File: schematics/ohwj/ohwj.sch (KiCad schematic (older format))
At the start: 11 parts

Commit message: Update power and labels; placing labels for all pins
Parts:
- removed C?: 1u, symbol Device:C_Small
- removed C?: 10n, symbol Device:C_Small
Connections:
- net labels added: BTN01, BTN02, BTN03, BTN04, BTN05, BTN06, BTN07, BTN08, BTN09, BTN10, BTN11, BTN12, BTN13, BTN14, BTN15, BTN16, GND, GPIO0, GPIO1, GPIO2, GPIO3, GPIO4, GPIO5, GPIO6, I2C_SCL, I2C_SDA, OSC_IN, OSC_OUT, SPI_MISO, SPI_MOSI, SPI_NSS, SPI_SCK, SWCLK, SWDIO, USART_RX, USART_TX, X0_ADC_IN0, X1_ADC_IN2, Y0_ADC_IN1, Y1_ADC_IN3
- net labels removed: VCC, VCCQ
- wire segments 47 -> 78
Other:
- note removed: "Power input for STM32F030C6 ADC"
- moved on the sheet: C?, D?, R?, SW?

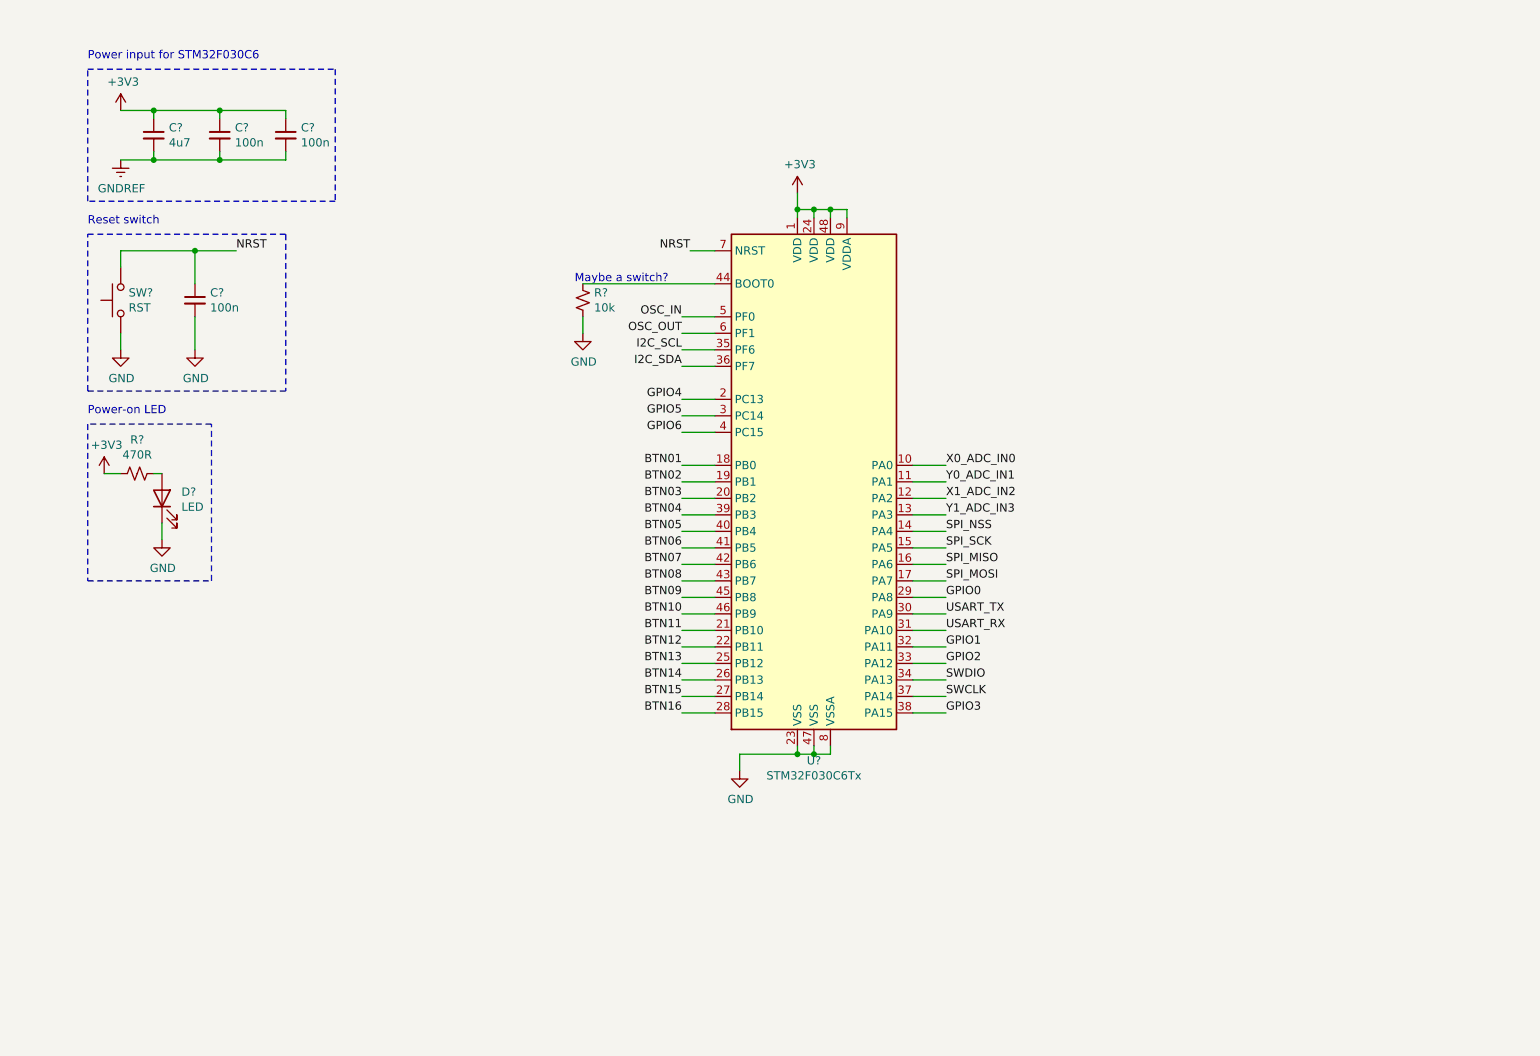
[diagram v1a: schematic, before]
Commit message: Add 8MHz crystal; assing component to pins (reset missing)
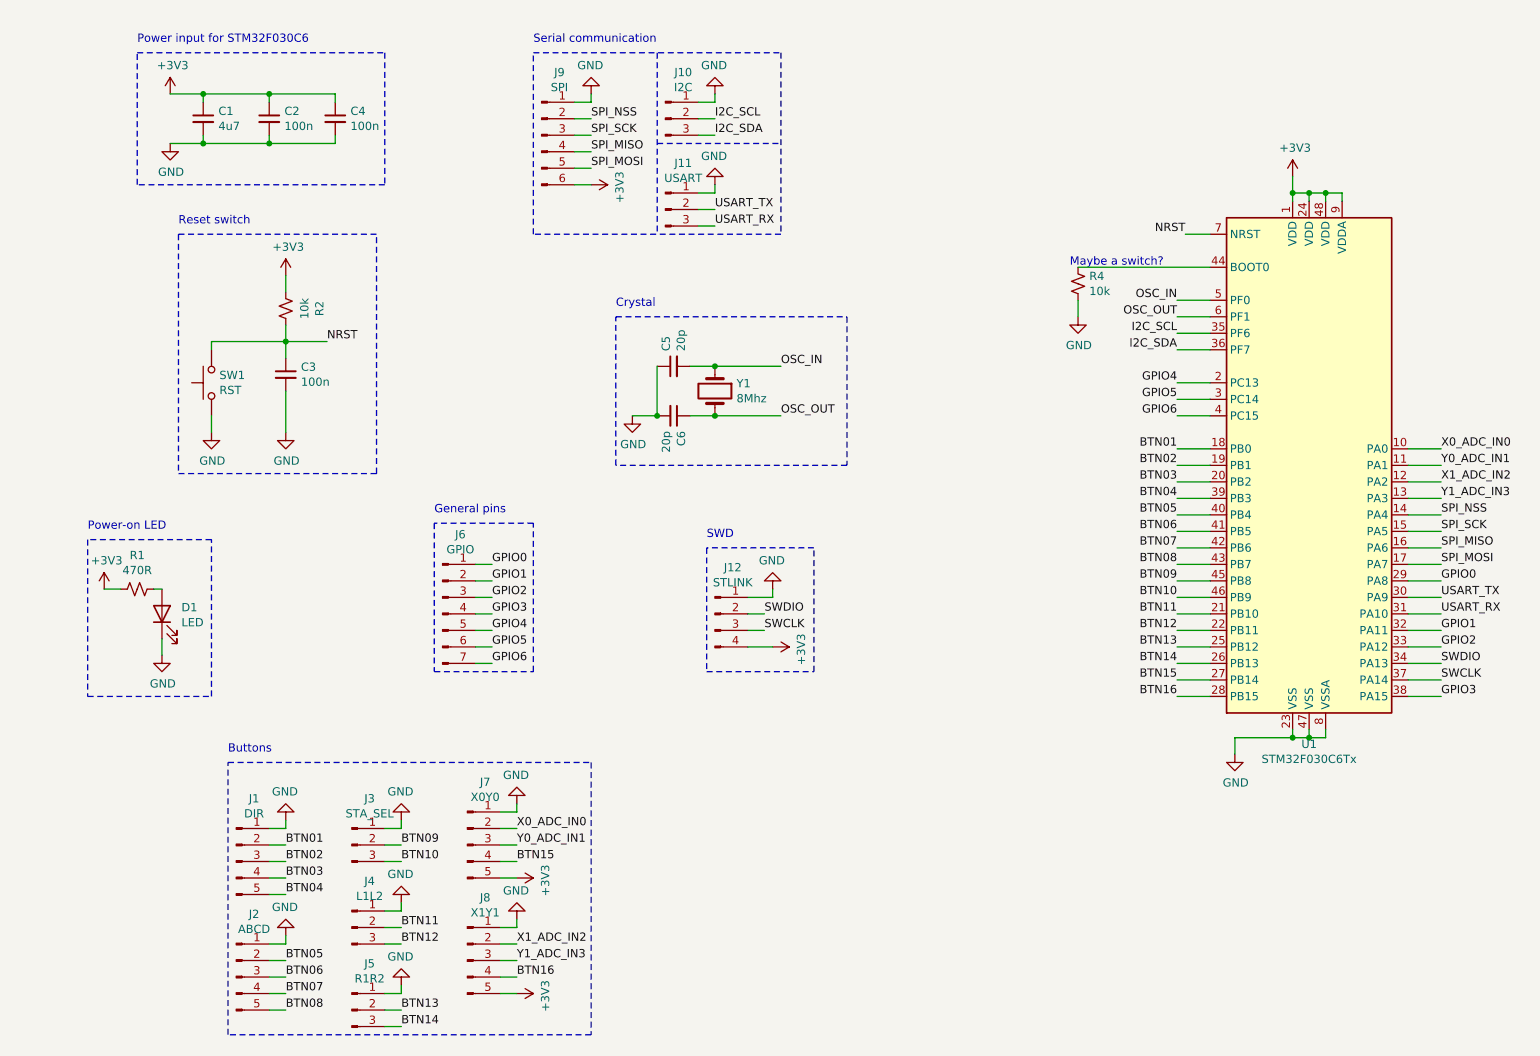
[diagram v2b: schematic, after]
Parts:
- added C5, C6: 20p, Capacitor_SMD:C_0603_1608Metric, symbol Device:C_Small
- added J1: DIR, Connector_PinHeader_2.54mm:PinHeader_1x05_P2.54mm_Vertical, symbol Connector:Conn_01x05_Male
- added J10: I2C, Connector_PinHeader_2.54mm:PinHeader_1x03_P2.54mm_Vertical, symbol Connector:Conn_01x03_Male
- added J11: USART, Connector_PinHeader_2.54mm:PinHeader_1x03_P2.54mm_Vertical, symbol Connector:Conn_01x03_Male
- added J12: STLINK, Connector_PinHeader_2.54mm:PinHeader_1x04_P2.54mm_Vertical, symbol Connector:Conn_01x04_Male
- added J2: ABCD, Connector_PinHeader_2.54mm:PinHeader_1x05_P2.54mm_Vertical, symbol Connector:Conn_01x05_Male
- added J3: STA_SEL, Connector_PinHeader_2.54mm:PinHeader_1x03_P2.54mm_Vertical, symbol Connector:Conn_01x03_Male
- added J4: L1L2, Connector_PinHeader_2.54mm:PinHeader_1x03_P2.54mm_Vertical, symbol Connector:Conn_01x03_Male
- added J5: R1R2, Connector_PinHeader_2.54mm:PinHeader_1x03_P2.54mm_Vertical, symbol Connector:Conn_01x03_Male
- added J6: GPIO, Connector_PinHeader_2.54mm:PinHeader_1x07_P2.54mm_Vertical, symbol Connector:Conn_01x07_Male
- added J7: X0Y0, Connector_PinHeader_2.54mm:PinHeader_1x05_P2.54mm_Vertical, symbol Connector:Conn_01x05_Male
- added J8: X1Y1, Connector_PinHeader_2.54mm:PinHeader_1x05_P2.54mm_Vertical, symbol Connector:Conn_01x05_Male
- added J9: SPI, Connector_PinHeader_2.54mm:PinHeader_1x06_P2.54mm_Vertical, symbol Connector:Conn_01x06_Male
- added R2: 10k, Resistor_SMD:R_0603_1608Metric, symbol Device:R_Small_US
- added Y1: 8Mhz, Crystal:Crystal_HC49-4H_Vertical, symbol Device:Crystal
- C1, C2, C3, C4: renamed from C?; footprint (none) -> Capacitor_SMD:C_0603_1608Metric
- D1: renamed from D?; footprint (none) -> LED_SMD:LED_0603_1608Metric
- R1, R4: renamed from R?; footprint (none) -> Resistor_SMD:R_0603_1608Metric
- gave numbers to parts that had none: 2
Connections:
- net GNDREF is gone; now on net GND: C1.2, C2.2, C4.2
- net +3V3: now also J12.4 (Pin_4), J7.5 (Pin_5), J8.5 (Pin_5), J9.6 (Pin_6), R2.1
- net BTN01: now also J1.2 (Pin_2)
- net BTN02: now also J1.3 (Pin_3)
- net BTN03: now also J1.4 (Pin_4)
- net BTN04: now also J1.5 (Pin_5)
- net BTN05: now also J2.2 (Pin_2)
- net BTN06: now also J2.3 (Pin_3)
- net BTN07: now also J2.4 (Pin_4)
- net BTN08: now also J2.5 (Pin_5)
- net BTN09: now also J3.2 (Pin_2)
- net BTN10: now also J3.3 (Pin_3)
- net BTN11: now also J4.2 (Pin_2)
- net BTN12: now also J4.3 (Pin_3)
- net BTN13: now also J5.2 (Pin_2)
- net BTN14: now also J5.3 (Pin_3)
- net BTN15: now also J7.4 (Pin_4)
- net BTN16: now also J8.4 (Pin_4)
- net GND: now also C5.1, C6.2, J1.1 (Pin_1), J10.1 (Pin_1), J11.1 (Pin_1), J12.1 (Pin_1), J2.1 (Pin_1), J3.1 (Pin_1), J4.1 (Pin_1), J5.1 (Pin_1), J7.1 (Pin_1), J8.1 (Pin_1), J9.1 (Pin_1)
- net GPIO0: now also J6.1 (Pin_1)
- net GPIO1: now also J6.2 (Pin_2)
- net GPIO2: now also J6.3 (Pin_3)
- net GPIO3: now also J6.4 (Pin_4)
- net GPIO4: now also J6.5 (Pin_5)
- net GPIO5: now also J6.6 (Pin_6)
- net GPIO6: now also J6.7 (Pin_7)
- net I2C_SCL: now also J10.2 (Pin_2)
- net I2C_SDA: now also J10.3 (Pin_3)
- net NRST: now also R2.2
- net OSC_IN: now also C5.2, Y1.1
- net OSC_OUT: now also C6.1, Y1.2
- net SPI_MISO: now also J9.4 (Pin_4)
- net SPI_MOSI: now also J9.5 (Pin_5)
- net SPI_NSS: now also J9.2 (Pin_2)
- net SPI_SCK: now also J9.3 (Pin_3)
- net SWCLK: now also J12.3 (Pin_3)
- net SWDIO: now also J12.2 (Pin_2)
- net USART_RX: now also J11.3 (Pin_3)
- net USART_TX: now also J11.2 (Pin_2)
- net X0_ADC_IN0: now also J7.2 (Pin_2)
- net X1_ADC_IN2: now also J8.2 (Pin_2)
- net Y0_ADC_IN1: now also J7.3 (Pin_3)
- net Y1_ADC_IN3: now also J8.3 (Pin_3)
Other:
- note added: "Buttons"
- note added: "Crystal"
- note added: "General pins"
- note added: "SWD"
- note added: "Serial communication"
- moved on the sheet: C1, C2, C3, C4, D1, R1, R4, SW1, U1

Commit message: Add voltage regulator; defined all footprints
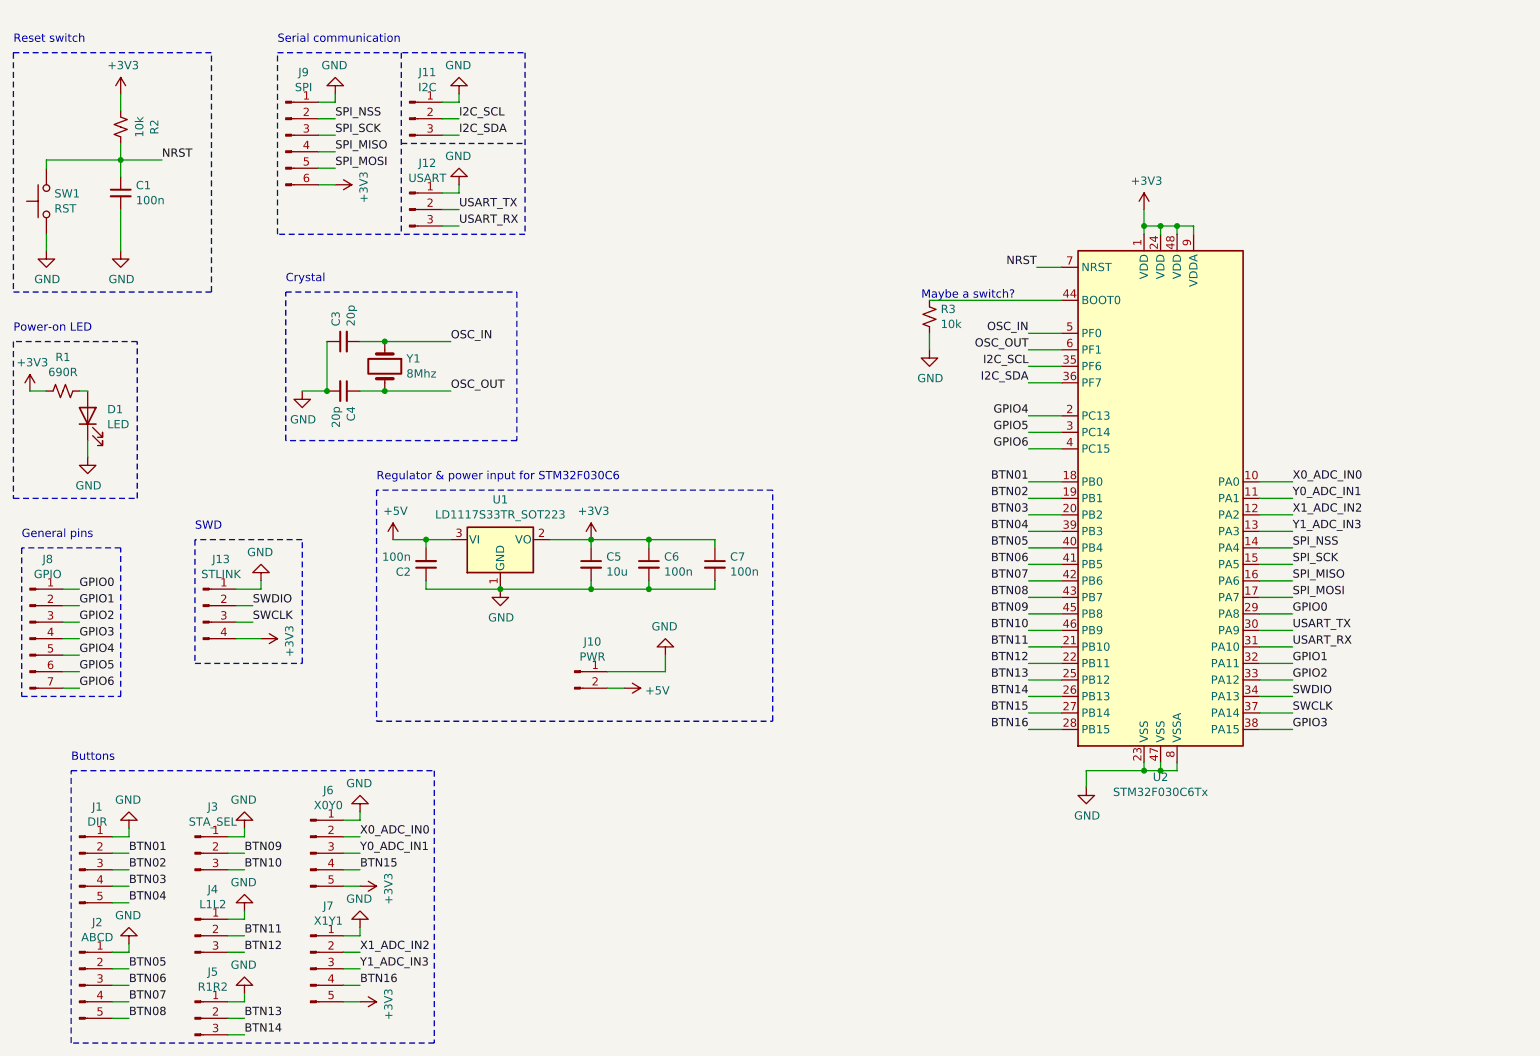
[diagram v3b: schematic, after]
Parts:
- removed C1: 4u7, Capacitor_SMD:C_0603_1608Metric, symbol Device:C_Small
- added C2: 100n, Capacitor_SMD:C_0603_1608Metric, symbol Device:C_Small
- added C5: 10u, Capacitor_SMD:C_0603_1608Metric, symbol Device:C_Small
- added J10: PWR, Connector_PinHeader_2.54mm:PinHeader_1x02_P2.54mm_Vertical, symbol Connector:Conn_01x02_Male
- added U1: LD1117S33TR_SOT223, Package_TO_SOT_SMD:SOT-223-3_TabPin2, symbol Regulator_Linear:LD1117S33TR_SOT223
- R1: value 470R -> 690R
- SW1: footprint (none) -> Button_Switch_THT:SW_PUSH_6mm_H4.3mm
- renumbered C3 to C1, C5 to C3, C6 to C4, C2 to C6, C4 to C7, J10 to J11, J11 to J12, J12 to J13, J7 to J6, J8 to J7, J6 to J8, R4 to R3, U1 to U2
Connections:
- net +3V3: now also C5.1, U1.2 (VO)
- net GND: now also C2.1, C5.2, J10.1 (Pin_1), U1.1 (GND)
- new net +5V: C2.2, J10.2 (Pin_2), U1.3 (VI)
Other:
- note added: "Regulator & power input for STM32F030C6"
- note removed: "Power input for STM32F030C6"
- moved on the sheet: C1, C3, C4, C6, C7, D1, J1, J11, J12, J13, J2, J3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

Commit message: Preliminar PCB layout
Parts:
- removed J1: DIR, Connector_PinHeader_2.54mm:PinHeader_1x05_P2.54mm_Vertical, symbol Connector:Conn_01x05_Male
- removed J11: I2C, Connector_PinHeader_2.54mm:PinHeader_1x03_P2.54mm_Vertical, symbol Connector:Conn_01x03_Male
- removed J12: USART, Connector_PinHeader_2.54mm:PinHeader_1x03_P2.54mm_Vertical, symbol Connector:Conn_01x03_Male
- removed J13: STLINK, Connector_PinHeader_2.54mm:PinHeader_1x04_P2.54mm_Vertical, symbol Connector:Conn_01x04_Male
- removed J2: ABCD, Connector_PinHeader_2.54mm:PinHeader_1x05_P2.54mm_Vertical, symbol Connector:Conn_01x05_Male
- removed J3: STA_SEL, Connector_PinHeader_2.54mm:PinHeader_1x03_P2.54mm_Vertical, symbol Connector:Conn_01x03_Male
- removed J4: L1L2, Connector_PinHeader_2.54mm:PinHeader_1x03_P2.54mm_Vertical, symbol Connector:Conn_01x03_Male
- removed J5: R1R2, Connector_PinHeader_2.54mm:PinHeader_1x03_P2.54mm_Vertical, symbol Connector:Conn_01x03_Male
- removed J6: X0Y0, Connector_PinHeader_2.54mm:PinHeader_1x05_P2.54mm_Vertical, symbol Connector:Conn_01x05_Male
- removed J7: X1Y1, Connector_PinHeader_2.54mm:PinHeader_1x05_P2.54mm_Vertical, symbol Connector:Conn_01x05_Male
- removed J8: GPIO, Connector_PinHeader_2.54mm:PinHeader_1x07_P2.54mm_Vertical, symbol Connector:Conn_01x07_Male
- removed J9: SPI, Connector_PinHeader_2.54mm:PinHeader_1x06_P2.54mm_Vertical, symbol Connector:Conn_01x06_Male
- added J1: SIDE A, Connector_PinHeader_2.54mm:PinHeader_1x06_P2.54mm_Vertical, symbol Connector:Conn_01x06_Male
- added J2: SIDE B, Connector_PinHeader_2.54mm:PinHeader_1x10_P2.54mm_Vertical, symbol Connector:Conn_01x10_Male
- added J3: SIDE C, Connector_PinHeader_2.54mm:PinHeader_1x12_P2.54mm_Vertical, symbol Connector:Conn_01x12_Male
- added J5: SIDE D, Connector_PinHeader_2.54mm:PinHeader_1x09_P2.54mm_Vertical, symbol Connector:Conn_01x09_Male
- renumbered J10 to J4
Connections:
- net BTN01: now also J2.6 (Pin_6)
- net BTN02: now also J2.7 (Pin_7)
- net BTN03: now also J2.8 (Pin_8)
- net BTN04: now also J5.3 (Pin_3)
- net BTN05: now also J5.4 (Pin_4)
- net BTN06: now also J5.5 (Pin_5)
- net BTN07: now also J5.6 (Pin_6)
- net BTN08: now also J5.7 (Pin_7)
- net BTN09: now also J5.8 (Pin_8)
- net BTN10: now also J5.9 (Pin_9)
- net BTN11: now also J2.9 (Pin_9)
- net BTN12: now also J2.10 (Pin_10)
- net BTN13: now also J3.1 (Pin_1)
- net BTN14: now also J3.2 (Pin_2)
- net BTN15: now also J3.3 (Pin_3)
- net BTN16: now also J3.4 (Pin_4)
- net GPIO0: now also J3.5 (Pin_5)
- net GPIO1: now also J3.8 (Pin_8)
- net GPIO2: now also J3.9 (Pin_9)
- net GPIO3: now also J5.2 (Pin_2)
- net SPI_MISO: now also J2.4 (Pin_4)
- net SPI_MOSI: now also J2.5 (Pin_5)
- net SPI_NSS: now also J2.2 (Pin_2)
- net SPI_SCK: now also J2.3 (Pin_3)
- net SWCLK: now also J5.1 (Pin_1)
- net SWDIO: now also J3.10 (Pin_10)
- net X0_ADC_IN0: now also J1.4 (Pin_4)
- net X1_ADC_IN2: now also J1.6 (Pin_6)
- net Y0_ADC_IN1: now also J1.5 (Pin_5)
- net Y1_ADC_IN3: now also J2.1 (Pin_1)
- net GPIO4 renamed PC13
- net PC13: now also J1.1 (Pin_1)
- net GPIO5 renamed PC14
- net PC14: now also J1.2 (Pin_2)
- net GPIO6 renamed PC15
- net PC15: now also J1.3 (Pin_3)
- net I2C_SCL renamed PF6
- net PF6: now also J3.11 (Pin_11)
- net I2C_SDA renamed PF7
- net PF7: now also J3.12 (Pin_12)
- net USART_RX renamed PA10
- net PA10: now also J3.7 (Pin_7)
- net USART_TX renamed PA9
- net PA9: now also J3.6 (Pin_6)
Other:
- note removed: "Buttons"
- note removed: "General pins"
- note removed: "SWD"
- note removed: "Serial communication"
- moved on the sheet: C2, C3, C4, C5, C6, C7, J4, U1, Y1
